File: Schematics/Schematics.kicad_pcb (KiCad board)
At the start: 2 copper layers, 8 parts, among them J1 Relay, J2 IR Sensor, J3 BB_I2C, U1 L7805, U2 ATtiny85-20PU

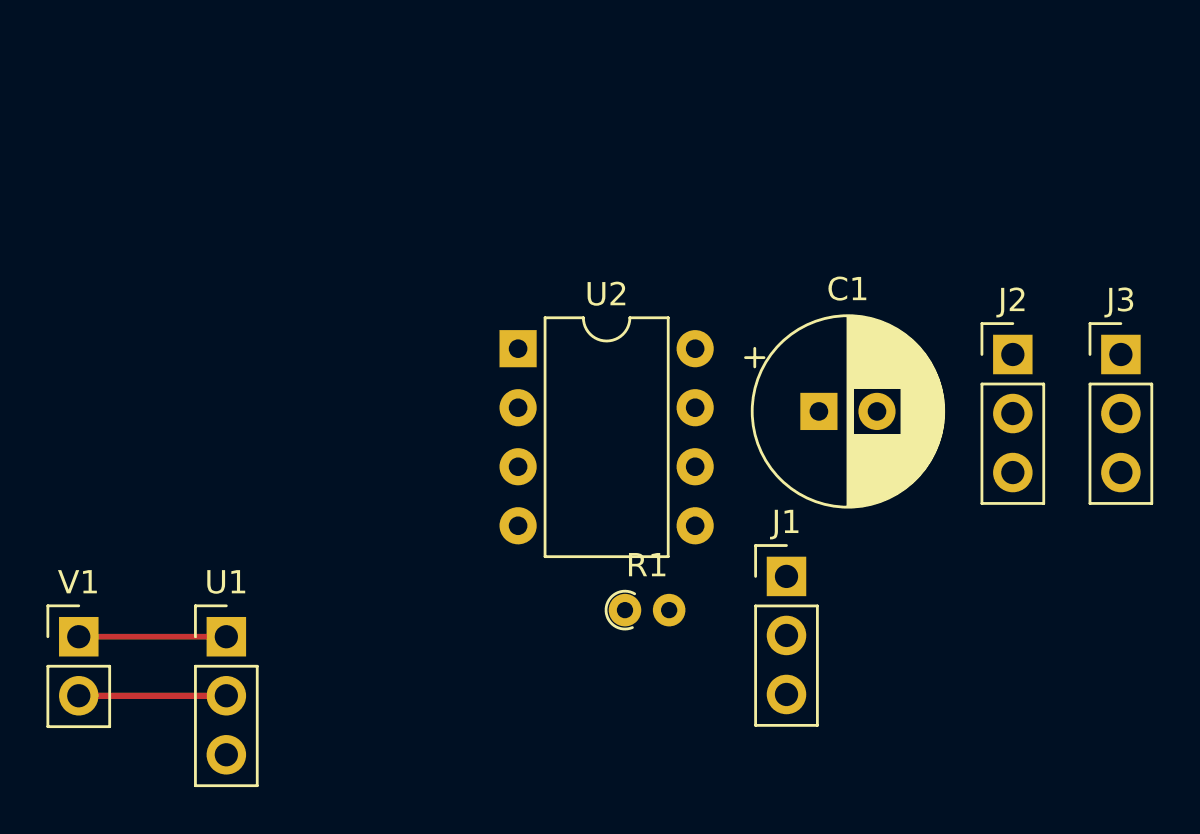
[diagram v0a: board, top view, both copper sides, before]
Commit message: The basic routes were finished.
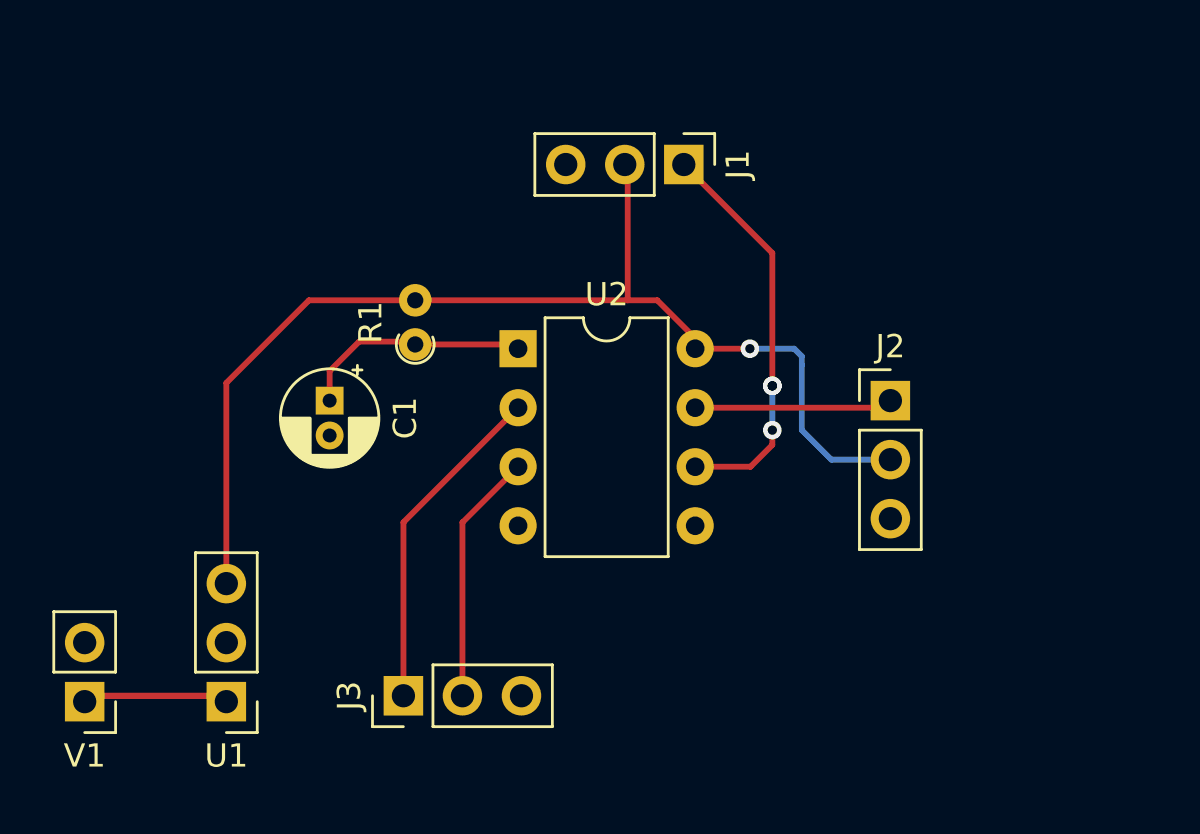
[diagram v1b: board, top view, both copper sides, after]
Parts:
- C1: footprint Capacitor_THT:CP_Radial_D8.0mm_P2.50mm -> Capacitor_THT:CP_Radial_D4.0mm_P1.50mm
- moved J3 34.2 mm to (94.0, 82.5), turned to 90 degrees
- moved C1 21.1 mm to (90.8, 69.8), turned to 270 degrees
- moved J1 18.3 mm to (106.0, 59.7), turned to 270 degrees
- moved R1 14.6 mm to (94.5, 67.4), turned to 90 degrees
- moved J2 5.63 mm to (114.9, 69.8)
- moved V1 2.81 mm to (80.3, 82.8), turned to 180 degrees
- moved U1 2.79 mm to (86.4, 82.8), turned to 180 degrees
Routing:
- net VCC: track 0.00 -> 49.3 mm, vias 0 -> 1
- net /Relay_Signal: track 0.00 -> 17.4 mm, vias 0 -> 3
- net /SCL: track 0.00 -> 14.4 mm
- net GND: track 11.9 -> 0.00 mm
- net /SDA: track 0.00 -> 10.8 mm
- net /RESET: track 0.00 -> 10.5 mm
- net /IR_Signal: track 0.00 -> 8.53 mm
- net Net-(U1-Pad1): track 6.35 -> 11.9 mm

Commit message: A silkscreen was added.
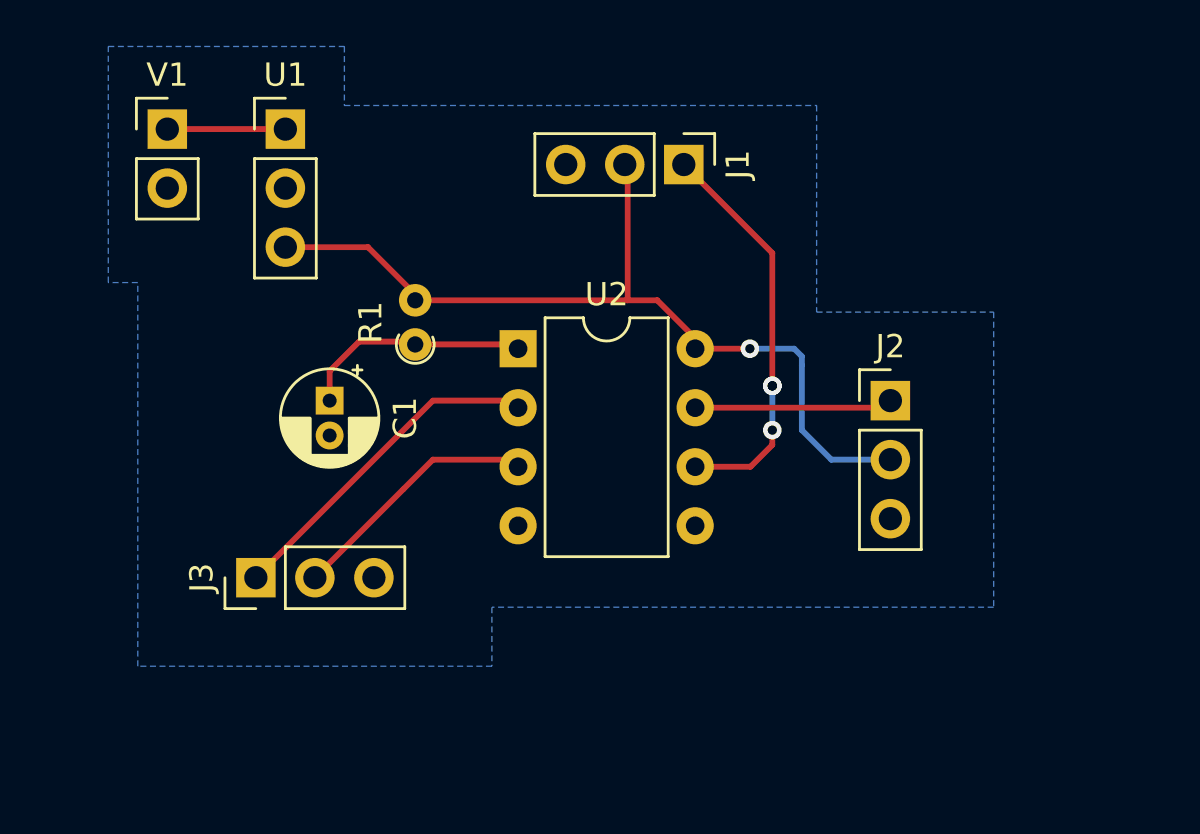
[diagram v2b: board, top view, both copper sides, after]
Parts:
- moved V1 24.9 mm to (83.8, 58.2), turned to 0 degrees
- moved U1 24.8 mm to (88.9, 58.2), turned to 0 degrees
- moved J3 8.13 mm to (87.6, 77.5)
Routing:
- net VCC: track 49.3 -> 37.7 mm
- net Net-(U1-Pad1): track 11.9 -> 5.19 mm
- added copper zone on B.Cu, net GND
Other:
- board text added: "+"
- board text added: "-"
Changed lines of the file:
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@@
   (general
     (thickness 1.6)
-    (drawings 0)
+    (drawings 2)
     (tracks 44)
     (zones 0)
@@
     (add_net GND)
     (add_net "Net-(U1-Pad1)")
-    (add_net "Net-(U2-Pad5)")
     (add_net VCC)
   )
@@
   )
   (module Connector_PinHeader_2.54mm:PinHeader_1x03_P2.54mm_Vertical (layer F.Cu)
-    (at 93.98 82.55 90)
+    (at 87.63 77.47 90)
     (descr "Through hole straight pin header, 1x03, 2.54mm pitch, single row")
     (tags "Through hole pin header THT 1x03 2.54mm single row")
@@
   )
   (module Connector_PinHeader_2.54mm:PinHeader_1x03_P2.54mm_Vertical (layer F.Cu)
-    (at 86.36 82.804 180)
+    (at 88.9 58.166)
     (descr "Through hole straight pin header, 1x03, 2.54mm pitch, single row")
     (tags "Through hole pin header THT 1x03 2.54mm single row")
@@
       (effects (font (size 1 1) (thickness 0.15)))
     )
-    (pad 3 thru_hole oval (at 0 5.08 180) (size 1.7 1.7) (drill 1) (layers *.Cu *.Mask)
+    (pad 3 thru_hole oval (at 0 5.08) (size 1.7 1.7) (drill 1) (layers *.Cu *.Mask)
       (net 3 VCC))
-    (pad 2 thru_hole oval (at 0 2.54 180) (size 1.7 1.7) (drill 1) (layers *.Cu *.Mask)
-      (net 2 GND))
-    (pad 1 thru_hole rect (at 0 0 180) (size 1.7 1.7) (drill 1) (layers *.Cu *.Mask)
+    (pad 2 thru_hole oval (at 0 2.54) (size 1.7 1.7) (drill 1) (layers *.Cu *.Mask)
+      (net 2 GND))
+    (pad 1 thru_hole rect (at 0 0) (size 1.7 1.7) (drill 1) (layers *.Cu *.Mask)
       (net 8 "Net-(U1-Pad1)"))
     (model ${KISYS3DMOD}/Connector_PinHeader_2.54mm.3dshapes/PinHeader_1x03_P2.54mm_Vertical.wrl
@@
   )
   (module Connector_PinHeader_2.54mm:PinHeader_1x02_P2.54mm_Vertical (layer F.Cu)
-    (at 80.264 82.804 180)
+    (at 83.82 58.166)
     (descr "Through hole straight pin header, 1x02, 2.54mm pitch, single row")
     (tags "Through hole pin header THT 1x02 2.54mm single row")
@@
       (effects (font (size 1 1) (thickness 0.15)))
     )
-    (pad 1 thru_hole rect (at 0 0 180) (size 1.7 1.7) (drill 1) (layers *.Cu *.Mask)
+    (pad 1 thru_hole rect (at 0 0) (size 1.7 1.7) (drill 1) (layers *.Cu *.Mask)
       (net 8 "Net-(U1-Pad1)"))
-    (pad 2 thru_hole oval (at 0 2.54 180) (size 1.7 1.7) (drill 1) (layers *.Cu *.Mask)
+    (pad 2 thru_hole oval (at 0 2.54) (size 1.7 1.7) (drill 1) (layers *.Cu *.Mask)
       (net 2 GND))
     (model ${KISYS3DMOD}/Connector_PinHeader_2.54mm.3dshapes/PinHeader_1x02_P2.54mm_Vertical.wrl
@@
       (rotate (xyz 0 0 0))
     )
+  )
+  (gr_text "-\n" (at 81.788 62.992) (layer Dwgs.User)
+    (effects (font (size 1 1) (thickness 0.15)))
+  )
+  (gr_text + (at 81.788 55.88) (layer Dwgs.User)
+    (effects (font (size 1 1) (thickness 0.15)))
   )
   (segment (start 94.488 67.432) (end 98.928 67.432) (width 0.25) (layer F.Cu) (net 1))
@@
   (segment (start 90.805 68.58) (end 92.075 67.31) (width 0.25) (layer F.Cu) (net 1))
   (segment (start 92.075 67.31) (end 94.615 67.31) (width 0.25) (layer F.Cu) (net 1))
-  (segment (start 86.36 82.55) (end 80.01 82.55) (width 0.25) (layer F.Cu) (net 8))
-  (segment (start 80.01 82.55) (end 85.559002 82.55) (width 0.25) (layer F.Cu) (net 8))
-  (segment (start 86.36 77.724) (end 86.36 69.088) (width 0.25) (layer F.Cu) (net 3))
-  (segment (start 86.36 69.088) (end 89.916 65.532) (width 0.25) (layer F.Cu) (net 3))
-  (segment (start 89.916 65.532) (end 94.488 65.532) (width 0.25) (layer F.Cu) (net 3))
   (segment (start 104.902 65.532) (end 106.68 67.31) (width 0.25) (layer F.Cu) (net 3))
   (segment (start 103.632 65.532) (end 103.632 59.817) (width 0.25) (layer F.Cu) (net 3))
@@
   (segment (start 111.125 71.12) (end 112.395 72.39) (width 0.25) (layer B.Cu) (net 3))
   (segment (start 112.395 72.39) (end 114.935 72.39) (width 0.25) (layer B.Cu) (net 3))
+  (segment (start 88.9 63.246) (end 92.456 63.246) (width 0.25) (layer F.Cu) (net 3))
+  (segment (start 92.456 63.246) (end 94.615 65.405) (width 0.25) (layer F.Cu) (net 3))
   (segment (start 106.535001 72.695001) (end 108.914999 72.695001) (width 0.25) (layer F.Cu) (net 4))
   (segment (start 108.914999 72.695001) (end 109.855 71.755) (width 0.25) (layer F.Cu) (net 4))
@@
   (segment (start 106.535001 70.155001) (end 114.629999 70.155001) (width 0.25) (layer F.Cu) (net 5))
   (segment (start 114.629999 70.155001) (end 114.935 69.85) (width 0.25) (layer F.Cu) (net 5))
-  (segment (start 98.915001 70.155001) (end 93.98 75.090002) (width 0.25) (layer F.Cu) (net 6))
-  (segment (start 93.98 75.090002) (end 93.98 82.55) (width 0.25) (layer F.Cu) (net 6))
-  (segment (start 98.915001 72.695001) (end 96.52 75.090002) (width 0.25) (layer F.Cu) (net 7))
-  (segment (start 96.52 75.090002) (end 96.52 82.55) (width 0.25) (layer F.Cu) (net 7))
+  (segment (start 87.63 77.47) (end 95.25 69.85) (width 0.25) (layer F.Cu) (net 6))
+  (segment (start 95.25 69.85) (end 99.06 69.85) (width 0.25) (layer F.Cu) (net 6))
+  (segment (start 90.17 77.47) (end 93.98 73.66) (width 0.25) (layer F.Cu) (net 7))
+  (segment (start 93.98 73.66) (end 95.25 72.39) (width 0.25) (layer F.Cu) (net 7))
+  (segment (start 95.25 72.39) (end 99.06 72.39) (width 0.25) (layer F.Cu) (net 7))
+  (segment (start 88.9 58.166) (end 84.074 58.166) (width 0.25) (layer F.Cu) (net 8))
+  (segment (start 84.074 58.166) (end 83.82 58.42) (width 0.25) (layer F.Cu) (net 8))
+  (zone (net 2) (net_name GND) (layer B.Cu) (hatch edge 0.508)
+    (connect_pads (clearance 0.508))
+    (min_thickness 0.254)
+    (fill yes (arc_segments 32) (thermal_gap 0.508) (thermal_bridge_width 0.508))
+    (polygon
+      (pts
+        (xy 91.44 57.15) (xy 111.76 57.15) (xy 111.76 66.04) (xy 119.38 66.04) (xy 119.38 78.74)
+        (xy 97.79 78.74) (xy 97.79 81.28) (xy 82.55 81.28) (xy 82.55 64.77) (xy 81.28 64.77)
+        (xy 81.28 54.61) (xy 91.44 54.61)
+      )
+    )
+  )
 )
